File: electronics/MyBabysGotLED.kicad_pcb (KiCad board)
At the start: 2 copper layers, 31 parts, among them J1 APA102, J3 Serial, P1 CONN_01X09, P2 CONN_01X09, P3 ATX_Power_2x12_Connector, Q1 PZT2222A, SW1 Reset, T1 CONN_01X01, T2 CONN_01X01, U1 ESP-13-WROOM-02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

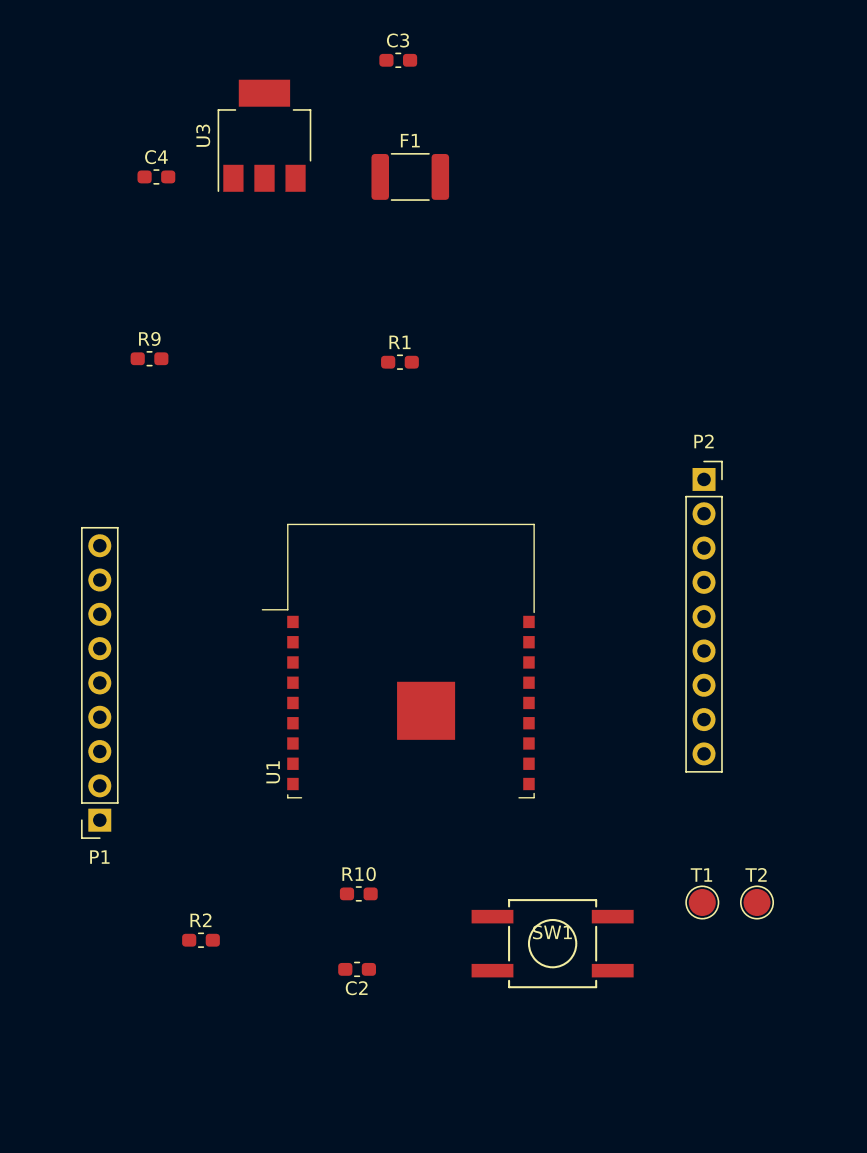
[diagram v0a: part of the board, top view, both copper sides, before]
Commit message: Most of BoM details added.  Part of #4
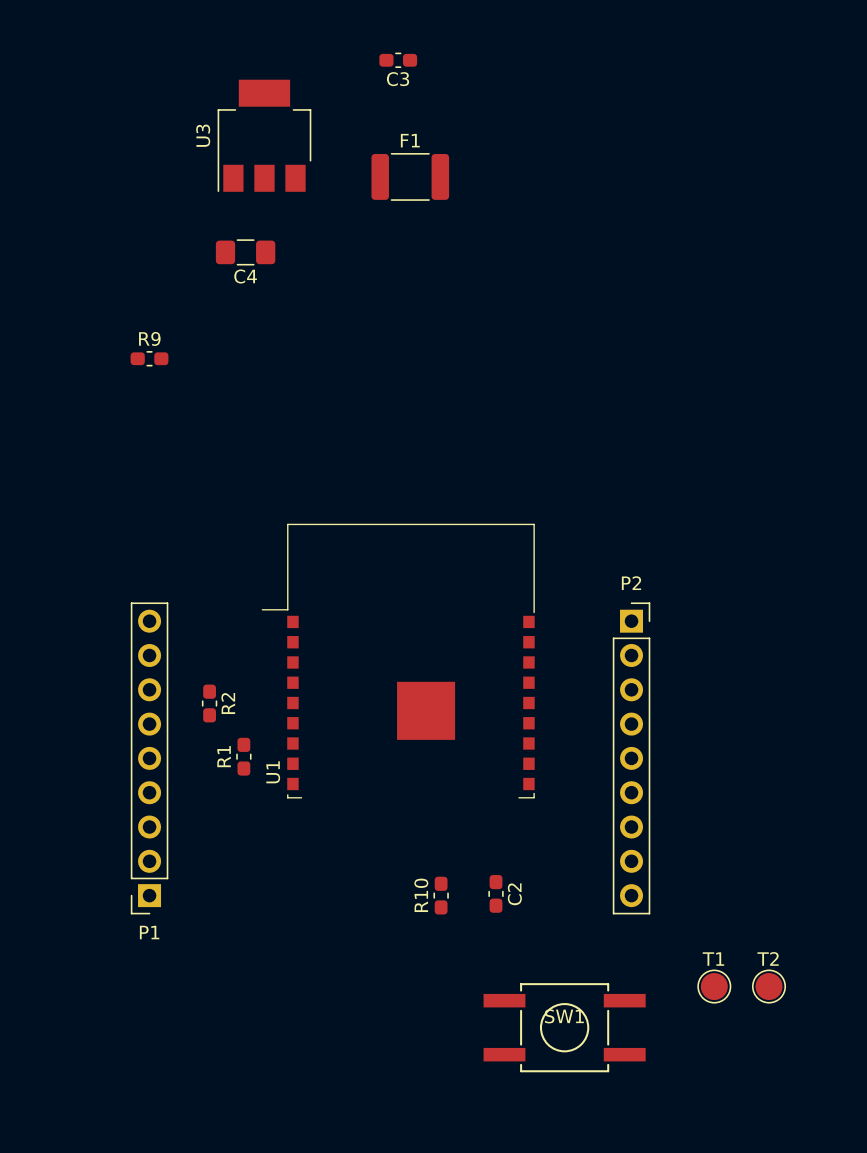
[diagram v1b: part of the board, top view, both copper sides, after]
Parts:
- C3: value 100nF -> 0.1uF
- C4: footprint Capacitor_SMD:C_0603_1608Metric_Pad1.05x0.95mm_HandSolder -> Capacitor_SMD:C_1206_3216Metric_Pad1.42x1.75mm_HandSolder
- Q1: value PZT2222A -> NJT4031NT1G
- moved R1 31.4 mm to (93.9, 125.3), turned to 90 degrees
- moved R2 17.5 mm to (91.3, 121.4), turned to 270 degrees
- moved P2 11.8 mm to (122.6, 115.3)
- moved C2 11.7 mm to (112.5, 135.5), turned to 270 degrees
- moved C4 8.65 mm to (94.0, 88.0), turned to 180 degrees
- moved P1 6.69 mm to (86.9, 135.6)
- moved SW1 6.29 mm to (117.6, 145.4)
- moved T2 6.29 mm to (132.7, 142.4)
- moved T1 6.29 mm to (128.7, 142.4)
- moved R10 6.10 mm to (108.5, 135.6), turned to 90 degrees
- turned C3 to 180 degrees

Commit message: PCB laid out.  Final part of #3 and all of #5
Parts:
- added F2: Fuse, mcqn-kicad-lib:Keystone_3557-2_Blade_Fuseholder, B.Cu at (150.4, 123.4)
- added G***: LOGO, mcqn-kicad-lib:mcqn-logo-30mm, B.Cu at (154.9, 66.0)
- added G***: LOGO, mcqn-kicad-lib:mcqn-logo-30mm, F.Cu at (154.9, 66.0)
- added J2: WS2812, Connector_PinHeader_2.54mm:PinHeader_1x03_P2.54mm_Vertical, F.Cu at (149.3, 103.0)
- added REF**: MountingHole_3.2mm_M3, MountingHole:MountingHole_3.2mm_M3, F.Cu at (167.7, 58.5)
- added REF**: LED_LIGHT_PIPE, mcqn-kicad-lib:LED_LIGHT_PIPE, F.Cu at (104.1, 113.0)
- added REF**: LED_LIGHT_PIPE, mcqn-kicad-lib:LED_LIGHT_PIPE, F.Cu at (104.1, 105.4)
- added REF**: MountingHole_3.2mm_M3, MountingHole:MountingHole_3.2mm_M3, F.Cu at (97.7, 58.5)
- added REF**: MountingHole_3.2mm_M3, MountingHole:MountingHole_3.2mm_M3, F.Cu at (167.7, 138.5)
- added REF**: MountingHole_3.2mm_M3, MountingHole:MountingHole_3.2mm_M3, F.Cu at (97.7, 138.5)
- added REF**: OSHW-Logo2_9.8x8mm_SilkScreen, Symbol:OSHW-Logo2_9.8x8mm_SilkScreen, B.Cu at (106.4, 90.2)
- added REF**: OSHW-Logo2_9.8x8mm_SilkScreen, Symbol:OSHW-Logo2_9.8x8mm_SilkScreen, F.Cu at (166.4, 130.8)
- added REF**: RoHS-Logo_6mm_SilkScreen, Symbol:RoHS-Logo_6mm_SilkScreen, B.Cu at (112.8, 82.5)
- added REF**: WEEE-Logo_4.2x6mm_SilkScreen, Symbol:WEEE-Logo_4.2x6mm_SilkScreen, B.Cu at (105.2, 74.9)
- added REF**: LED_LIGHT_PIPE, mcqn-kicad-lib:LED_LIGHT_PIPE, F.Cu at (104.1, 120.7)
- J1: footprint Connector_Phoenix_MSTB:PhoenixContact_MSTBVA_2,5_5-G-5,08_1x05_P5.08mm_Vertical -> Connector_Phoenix_MSTB:PhoenixContact_MSTBVA_2,5_4-G-5,08_1x04_P5.08mm_Vertical
- moved C5 102.6 mm to (127.6, 61.0)
- moved J1 99.9 mm to (159.3, 90.7), turned to 270 degrees
- moved U2 95.4 mm to (130.9, 66.9), turned to 90 degrees
- moved P3 94.3 mm to (136.5, 107.3), turned to 90 degrees
- moved R4 91.6 mm to (137.4, 73.4), turned to 270 degrees
- moved R3 83.3 mm to (132.1, 73.4)
- moved J3 78.0 mm to (106.7, 59.7), turned to 90 degrees
- moved R5 75.9 mm to (111.8, 113.0)
- moved Q1 72.4 mm to (120.7, 110.5)
- moved U3 61.9 mm to (123.7, 134.4), turned to 270 degrees
- moved C2 61.6 mm to (119.8, 74.3), turned to 0 degrees
- moved R10 59.5 mm to (119.8, 77.2), turned to 180 degrees
- moved C3 57.9 mm to (125.0, 128.3), turned to 0 degrees
- moved C4 57.3 mm to (129.3, 133.1), turned to 90 degrees
- moved C1 53.9 mm to (162.6, 123.2), turned to 90 degrees
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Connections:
- J1 pad 1: Net-(C1-Pad1) -> GND
- J1 pad 4: GND -> Net-(C1-Pad1)
- R3 pad 2: Net-(J1-Pad2) -> Net-(J1-Pad3)
- R4 pad 2: Net-(J1-Pad3) -> Net-(J1-Pad2)
- U2 pad 2: LED_Data -> LED_Clk
- U2 pad 5: LED_Clk -> LED_Data
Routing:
- net GND: track 0.00 -> 363.8 mm, vias 0 -> 4
- net Net-(C1-Pad1): track 0.00 -> 134.4 mm
- net +3V3: track 0.00 -> 103.3 mm
- net /BaseESP8266/RST: track 0.00 -> 95.7 mm
- net /BaseESP8266/IO4: track 0.00 -> 94.6 mm
- net Net-(F1-Pad2): track 0.00 -> 85.3 mm
- net Net-(J1-Pad3): track 0.00 -> 66.4 mm
- net Net-(J1-Pad2): track 0.00 -> 65.5 mm
- net LED_Data: track 0.00 -> 58.3 mm, vias 0 -> 3
- net Net-(P3-Pad1): track 0.00 -> 54.8 mm, vias 0 -> 2
- net +5V: track 0.00 -> 47.9 mm
- net LED_Clk: track 0.00 -> 40.6 mm, vias 0 -> 3
- net Net-(P3-Pad16): track 0.00 -> 36.3 mm, vias 0 -> 2
- net /BaseESP8266/IO13: track 0.00 -> 33.7 mm, vias 0 -> 1
- net /BaseESP8266/IO12: track 0.00 -> 30.3 mm, vias 0 -> 1
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- added copper zone on F.Cu, net +3V3
- added copper zone on B.Cu, net +5V
- added copper zone on F.Cu, net +5V
- added copper zone on B.Cu, net GND
- added copper zone on F.Cu, net GND
- added copper zone on B.Cu, net Net-(C1-Pad1)
- added copper zone on F.Cu, net Net-(C1-Pad1)
- added copper zone on F.Cu, net Net-(C3-Pad1)
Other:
- board outline added: 80 x 90 mm
- board text added: "#BornInLiverpool"
- board text added: "0"
- board text added: "12"
- board text added: "13"
- board text added: "14"
- board text added: "15"
- board text added: "16"
- board text added: "2"
- board text added: "4"
- board text added: "5"
- board text added: "5V"
- board text added: "5V SB"
- board text added: "Clk"
- board text added: "Data"
- board text added: "EN"
- board text added: "GND"
- board text added: "Gnd"
- board text added: "LED Connections"
- board text added: "LED Power"
- board text added: "Network"
- board text added: "RST"
- board text added: "RX"
- board text added: "Reset"
- board text added: "Serial"
- board text added: "TOUT"
- board text added: "TX"
- board text added: "VCC"
- board text added: "WiFi"
- board text added: "mcqn.com/ibal223"
- board text added: "r20201104"

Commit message: Board mods to use lower value fuses (rather than a single large fuse).  Fixes #14
* Three 5V/Gnd feeds rather than one, each protected with a 5x20mm 8A fuse
* 470uF smoothing caps on the 5V lines, rather than a single 1000uF
* New test points for 5V, data and clock lines
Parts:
- removed the G*** at (154.9, 66.0) (x2)
- removed the REF** at (167.7, 58.5)
- removed the REF** at (104.1, 113.0)
- removed the REF** at (104.1, 105.4)
- removed the REF** at (167.7, 138.5)
- removed the REF** at (106.4, 90.2)
- removed the REF** at (166.4, 130.8)
- removed the REF** at (105.2, 74.9)
- removed the REF** at (104.1, 120.7)
- added 5V_T1: Conn_01x01, TestPoint:TestPoint_Pad_D2.0mm, F.Cu at (139.2, 62.0)
- added C6: 470uF, Capacitor_SMD:C_Elec_10x10.2, B.Cu at (151.5, 95.8)
- added C7: 470uF, Capacitor_SMD:C_Elec_10x10.2, B.Cu at (175.6, 95.8)
- added Clk_T1: Conn_01x01, TestPoint:TestPoint_Pad_D2.0mm, F.Cu at (139.2, 68.8)
- added Data_T1: Conn_01x01, TestPoint:TestPoint_Pad_D2.0mm, F.Cu at (146.1, 76.7)
- added F3: Fuse, mcqn-kicad-lib:Fuseholder_Cylinder-5x20mm_Wurth_WR-FSH_Horizontal, B.Cu at (153.0, 133.9)
- added F4: Fuse, mcqn-kicad-lib:Fuseholder_Cylinder-5x20mm_Wurth_WR-FSH_Horizontal, B.Cu at (153.2, 122.3)
- added G***: LOGO, mcqn-kicad-lib:mcqn-logo-30mm, B.Cu at (189.2, 64.8)
- added G***: LOGO, mcqn-kicad-lib:mcqn-logo-30mm, F.Cu at (189.2, 64.8)
- added PWR_ON_T1: Conn_01x01, TestPoint:TestPoint_Pad_D2.0mm, F.Cu at (126.5, 105.9)
- added REF**: MountingHole_3.2mm_M3, MountingHole:MountingHole_3.2mm_M3, F.Cu at (207.7, 138.5)
- added REF**: MountingHole_3.2mm_M3, MountingHole:MountingHole_3.2mm_M3, F.Cu at (207.7, 58.5)
- added REF**: WEEE-Logo_5.6x8mm_SilkScreen, Symbol:WEEE-Logo_5.6x8mm_SilkScreen, B.Cu at (98.8, 109.0)
- added REF**: OSHW-Logo2_14.6x12mm_SilkScreen, Symbol:OSHW-Logo2_14.6x12mm_SilkScreen, B.Cu at (101.6, 127.5)
- added REF**: OSHW-Logo2_14.6x12mm_SilkScreen, Symbol:OSHW-Logo2_14.6x12mm_SilkScreen, F.Cu at (195.3, 136.4)
- C1: value 1000uF -> 470uF; footprint mcqn-kicad-lib:c_elec_12.5x12.5 -> Capacitor_SMD:C_Elec_10x10.2
- F2: footprint mcqn-kicad-lib:Keystone_3557-2_Blade_Fuseholder -> mcqn-kicad-lib:Fuseholder_Cylinder-5x20mm_Wurth_WR-FSH_Horizontal
- J1: footprint Connector_Phoenix_MSTB:PhoenixContact_MSTBVA_2,5_4-G-5,08_1x04_P5.08mm_Vertical -> Connector_Phoenix_MSTB:PhoenixContact_MSTBVA_2,5_8-G-5,08_1x08_P5.08mm_Vertical
- moved J1 40.4 mm to (199.1, 84.5)
- moved J2 37.5 mm to (186.8, 104.8)
- moved REF** 35.5 mm to (106.9, 117.6)
- moved C1 27.5 mm to (163.6, 95.8)
- moved F2 13.0 mm to (153.2, 110.7), turned to 0 degrees
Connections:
- C5 pad 1: Net-(C1-Pad1) -> Net-(5V_T1-Pad1)
- F2 pad 2: Net-(C1-Pad1) -> Net-(5V_T1-Pad1)
- J1 pad 2: Net-(J1-Pad2) -> GND
- J1 pad 3: Net-(J1-Pad3) -> GND
- J1 pad 4: Net-(C1-Pad1) -> Net-(Data_T1-Pad1)
- J2 pad 1: Net-(C1-Pad1) -> Net-(5V_T1-Pad1)
- J2 pad 2: Net-(J1-Pad2) -> Net-(Data_T1-Pad1)
- R3 pad 2: Net-(J1-Pad3) -> Net-(Clk_T1-Pad1)
- R4 pad 2: Net-(J1-Pad2) -> Net-(Data_T1-Pad1)
- U2 pad 14: Net-(C1-Pad1) -> Net-(5V_T1-Pad1)
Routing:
- net Net-(5V_T1-Pad1): track 0.00 -> 198.6 mm
- net Net-(Data_T1-Pad1): track 0.00 -> 113.5 mm
- net Net-(Clk_T1-Pad1): track 0.00 -> 111.0 mm
- net Net-(C6-Pad1): track 0.00 -> 80.3 mm
- net Net-(C1-Pad1): track 134.4 -> 54.2 mm
- net Net-(J1-Pad3): track 66.4 -> 0.00 mm
- net Net-(J1-Pad2): track 65.5 -> 0.00 mm
- net +5V: track 47.9 -> 81.3 mm
- net GND: track 363.8 -> 346.1 mm
- net Net-(P3-Pad16): track 36.3 -> 42.3 mm
- net +3V3: track 103.3 -> 98.1 mm
- added copper zone on B.Cu, net Net-(5V_T1-Pad1)
- added copper zone on F.Cu, net Net-(5V_T1-Pad1)
- added copper zone on B.Cu, net Net-(C6-Pad1)
- added copper zone on F.Cu, net Net-(C6-Pad1)
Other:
- board size 80 x 90 mm -> 120 x 90 mm
- board text added: "r20210224"
- board text removed: "r20201104"
